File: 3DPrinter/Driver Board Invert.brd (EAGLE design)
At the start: 127.6 x 42.2 mm, 21 parts, among them X1 CON-7.62-02P, X2 CON-XH-04

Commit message: _
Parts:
- removed IC1: (no value), Flamberm:DRV-ST820-REV
- removed JP2: (no value), pinhead:1X04
- removed R1, R2, R3: 15K, Flamberm:RESC2012X50
- removed S1: (no value), Namenlos:DIP03YL
- removed X2: CON-XH-04, Namenlos:XH-04
- added IC2, IC3, IC5, IC7, IC9: (no value), Flamberm:DRV-ST820-REV
- added JP11, JP3, JP4, JP6, JP9: (no value), pinhead:1X04
- added R13, R14, R15, R24, R25, R26, R30, R31, R32, R4, R5, R6, R7, R8, R9: 15K, Flamberm:RESC2012X50
- added S2, S3, S5, S7, S9: (no value), Namenlos:DIP03YL
- added X10, X3, X4, X6, X8: CON-XH-04, Namenlos:XH-04
- moved C3 20.9 mm to (-3.17, 41.9), turned to 270 degrees
- moved X1 19.7 mm to (-6.99, 71.1)
- moved JP7 19.1 mm to (-9.91, 41.3)
- moved JP1 13.5 mm to (10.2, 41.3)
- moved C1 13.4 mm to (-3.17, 54.0)
- moved D1 13.4 mm to (-8.89, 56.5)
- moved L1 13.4 mm to (-8.89, 50.2)
- moved R16 13.4 mm to (-0.51, 59.1)
- moved R19 13.4 mm to (-5.71, 50.8)
- moved R20 13.4 mm to (-2.54, 49.5)
- moved C2 13.4 mm to (-1.27, 54.0)
- moved R17 13.4 mm to (-1.91, 59.1)
- moved R18 13.4 mm to (-3.30, 59.1)
- moved U$1 13.4 mm to (-1.91, 57.1)
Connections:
- removed net N$1: IC1.EN, JP2.1
- removed net N$12: IC1.2A, X2.3
- removed net N$13: IC1.1A, X2.4
- removed net N$2: IC1.STEP, JP2.2
- removed net N$3: IC1.DIR, JP2.3
- removed net N$4: IC1.1B, X2.1
- removed net N$5: IC1.MS0, R3.2, S1.1
- removed net N$6: IC1.MS1, R2.2, S1.2
- removed net N$7: IC1.MS2, R1.2, S1.3
- removed net N$8: IC1.2B, X2.2
- new net N$10: IC2.STEP, JP3.2
- new net N$11: IC2.DIR, JP3.3
- new net N$14: IC2.1B, X3.1
- new net N$15: IC2.2B, X3.2
- new net N$16: IC2.2A, X3.3
- new net N$17: IC2.1A, X3.4
- new net N$18: IC2.MS0, R6.2, S2.1
- new net N$19: IC2.MS1, R5.2, S2.2
- new net N$20: IC2.MS2, R4.2, S2.3
- new net N$21: IC3.EN, JP4.1
- new net N$22: IC3.STEP, JP4.2
- new net N$23: IC3.DIR, JP4.3
- new net N$24: IC3.1B, X4.1
- new net N$25: IC3.2B, X4.2
- new net N$26: IC3.2A, X4.3
- new net N$27: IC3.1A, X4.4
- new net N$28: IC3.MS0, R9.2, S3.1
- new net N$29: IC3.MS1, R8.2, S3.2
- new net N$30: IC3.MS2, R7.2, S3.3
- new net N$41: IC5.EN, JP6.1
- new net N$42: IC5.STEP, JP6.2
- new net N$43: IC5.DIR, JP6.3
- new net N$44: IC5.1B, X6.1
- new net N$45: IC5.2B, X6.2
- new net N$46: IC5.2A, X6.3
- new net N$47: IC5.1A, X6.4
- new net N$48: IC5.MS0, R15.2, S5.1
- new net N$49: IC5.MS1, R14.2, S5.2
- new net N$50: IC5.MS2, R13.2, S5.3
- new net N$65: IC7.EN, JP9.1
- new net N$66: IC7.STEP, JP9.2
- new net N$67: IC7.DIR, JP9.3
- new net N$68: IC7.1B, X8.1
- new net N$69: IC7.2B, X8.2
- new net N$70: IC7.2A, X8.3
- new net N$71: IC7.1A, X8.4
- new net N$72: IC7.MS0, R26.2, S7.1
- new net N$73: IC7.MS1, R25.2, S7.2
- new net N$74: IC7.MS2, R24.2, S7.3
- new net N$85: IC9.EN, JP11.1
- new net N$86: IC9.STEP, JP11.2
- new net N$87: IC9.DIR, JP11.3
- new net N$88: IC9.1B, X10.1
- new net N$89: IC9.2B, X10.2
- new net N$9: IC2.EN, JP3.1
- new net N$90: IC9.2A, X10.3
- new net N$91: IC9.1A, X10.4
- new net N$92: IC9.MS0, R32.2, S9.1
- new net N$93: IC9.MS1, R31.2, S9.2
- new net N$94: IC9.MS2, R30.2, S9.3
- net +24V: now also IC2.VM, IC3.VM, IC5.VM, IC7.VM, IC9.VM; no longer IC1.VM
- net +3V3: now also IC2.VDD, IC3.VDD, IC5.VDD, IC7.VDD, IC9.VDD, S2.4, S2.5, S2.6, S3.4, S3.5, S3.6, S5.4, S5.5, S5.6, S7.4, S7.5, S7.6, S9.4, S9.5, S9.6; no longer IC1.VDD, S1.4, S1.5, S1.6
- net GND: now also IC2.GND@1, IC2.GND@2, IC3.GND@1, IC3.GND@2, IC5.GND@1, IC5.GND@2, IC7.GND@1, IC7.GND@2, IC9.GND@1, IC9.GND@2, JP11.4, JP3.4, JP4.4, JP6.4, JP9.4, R13.1, R14.1, R15.1, R24.1, R25.1, R26.1, R30.1, R31.1, R32.1, R4.1, R5.1, R6.1, R7.1, R8.1, R9.1; no longer IC1.GND@1, IC1.GND@2, JP2.4, R1.1, R2.1, R3.1
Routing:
- net GND: track 132.5 -> 464.3 mm, vias 2 -> 0
- net +3V3: track 34.4 -> 229.7 mm
- net +24V: track 19.7 -> 208.0 mm, vias 0 -> 10
- net N$1: track 17.8 -> 0.00 mm
- net N$65: track 0.00 -> 15.8 mm
- net N$9: track 0.00 -> 15.8 mm
- net N$85: track 0.00 -> 15.8 mm
- net N$41: track 0.00 -> 15.8 mm
- net N$21: track 0.00 -> 15.8 mm
- net N$91: track 0.00 -> 7.01 mm
- net N$88: track 0.00 -> 7.01 mm
- net N$71: track 0.00 -> 7.01 mm
- net N$47: track 0.00 -> 7.01 mm
- net N$44: track 0.00 -> 7.01 mm
- net N$4: track 7.01 -> 0.00 mm
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- added copper zone on layer 16, net GND
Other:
- board size 127.6 x 42.2 mm -> 140.9 x 42.2 mm

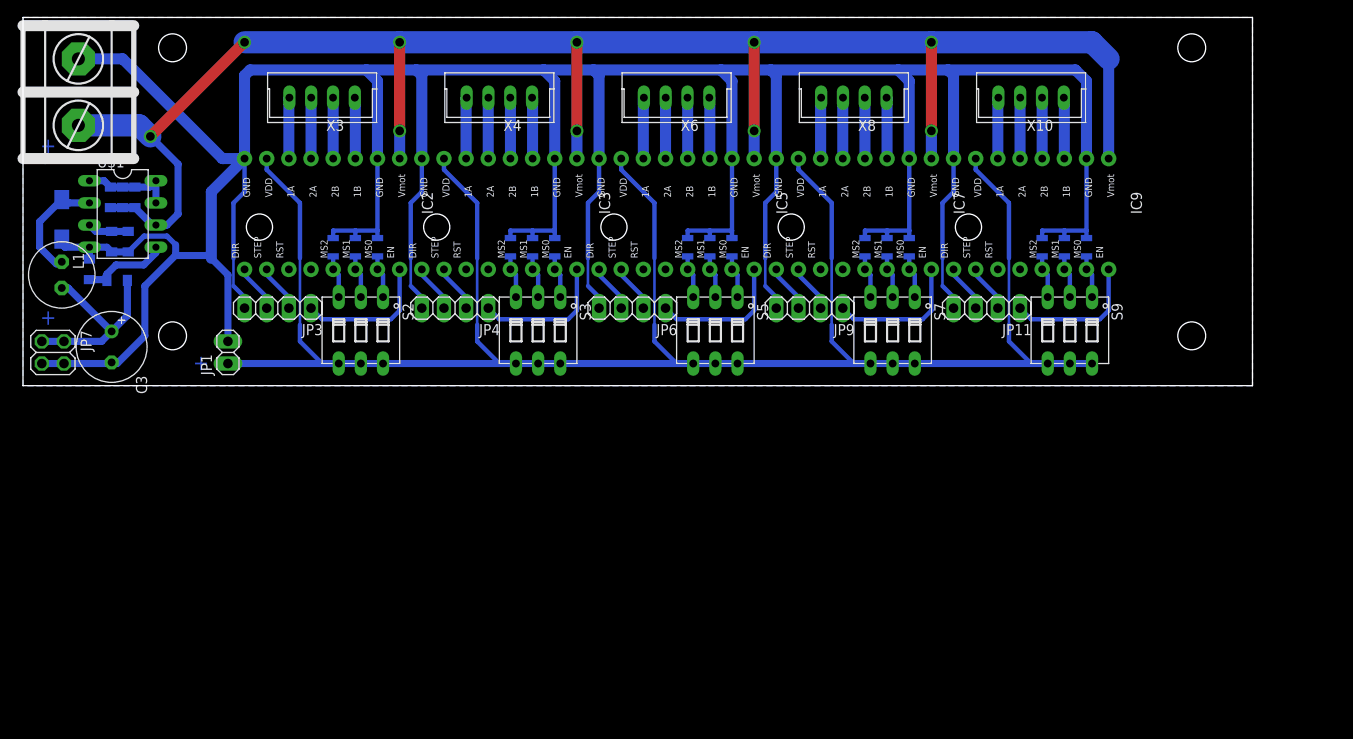
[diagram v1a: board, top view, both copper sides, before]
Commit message: Inverted Driver Board
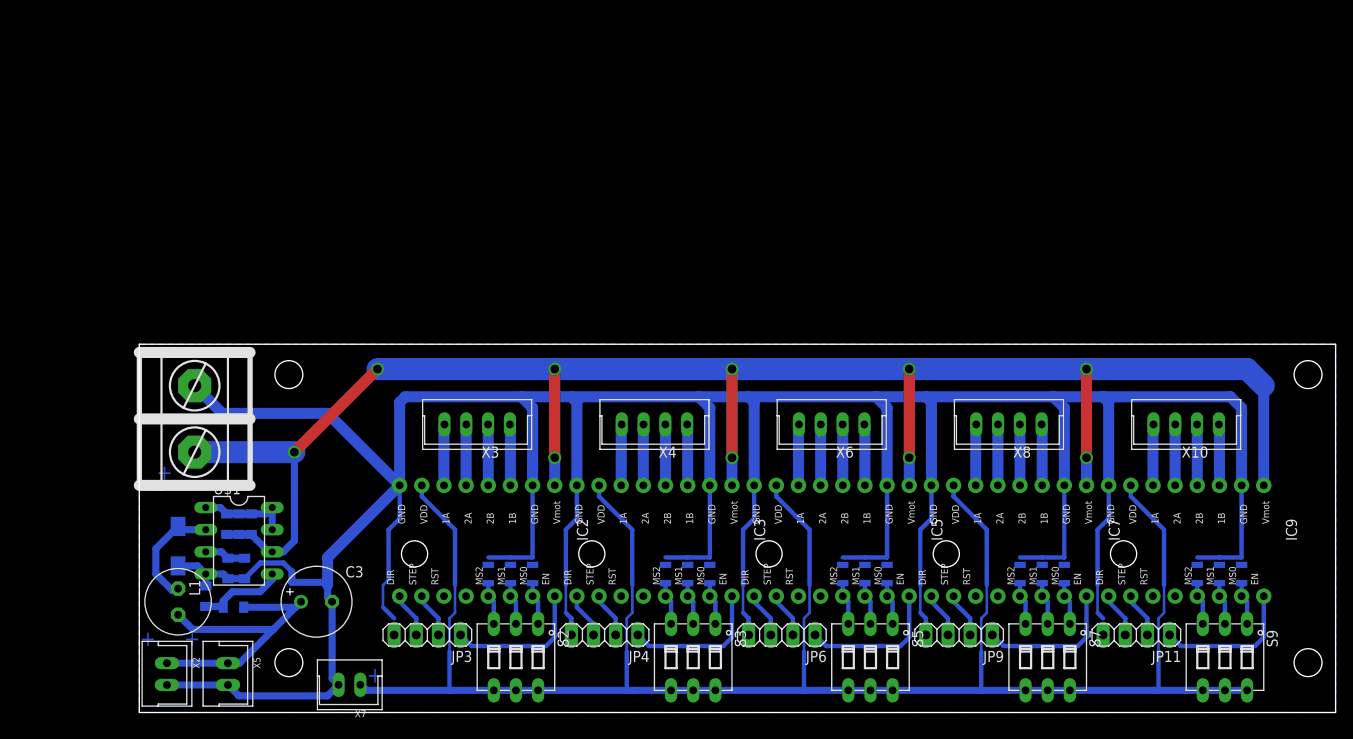
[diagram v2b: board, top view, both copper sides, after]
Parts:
- removed JP1: (no value), pinhead:1X02
- removed JP7: (no value), pinhead:2X02
- added X2, X5, X7: CON-XH-02, Flamberm:XH-02
- moved IC2 41.5 mm to (38.7, 19.7)
- moved IC3 41.5 mm to (59.1, 19.7)
- moved IC5 41.5 mm to (79.4, 19.7)
- moved IC9 41.5 mm to (120.0, 19.7)
- moved R14 41.5 mm to (83.2, 15.9)
- moved R15 41.5 mm to (85.7, 15.9)
- moved R24 41.5 mm to (101.0, 15.9)
- moved R25 41.5 mm to (103.5, 15.9)
- moved R26 41.5 mm to (106.0, 15.9)
- moved R30 41.5 mm to (121.3, 15.9)
- moved R31 41.5 mm to (123.8, 15.9)
- moved R32 41.5 mm to (126.4, 15.9)
- moved R4 41.5 mm to (40.0, 15.9)
- moved R5 41.5 mm to (42.5, 15.9)
- moved R6 41.5 mm to (45.1, 15.9)
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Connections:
- net +12V: now also X2.1, X5.1; no longer JP7.1, JP7.2
- net +3V3: now also X7.1; no longer JP1.1
- net GND: now also X2.2, X5.2, X7.2; no longer JP1.2, JP7.3, JP7.4
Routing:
- net +12V: track 22.8 -> 36.9 mm
- net GND: track 464.3 -> 451.3 mm
- net +24V: track 208.0 -> 211.3 mm
- net N$85: track 15.8 -> 16.5 mm
- net N$41: track 15.8 -> 16.5 mm
- net N$9: track 15.8 -> 16.5 mm
- net N$21: track 15.8 -> 16.5 mm
- net N$65: track 15.8 -> 16.5 mm
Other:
- board size 140.9 x 42.2 mm -> 137.1 x 42.2 mm
